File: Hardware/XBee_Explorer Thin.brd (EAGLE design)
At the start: 43.2 x 52.1 mm, 65 parts, among them J4 QWIIC_RIGHT_ANGLE, Q2 3.1A/30V/105mΩ, U1 FSUSB30MUX_MSOP10, U2 AP63203, U3 ESD Diode, U5 ESD Diode, U6 CP210X

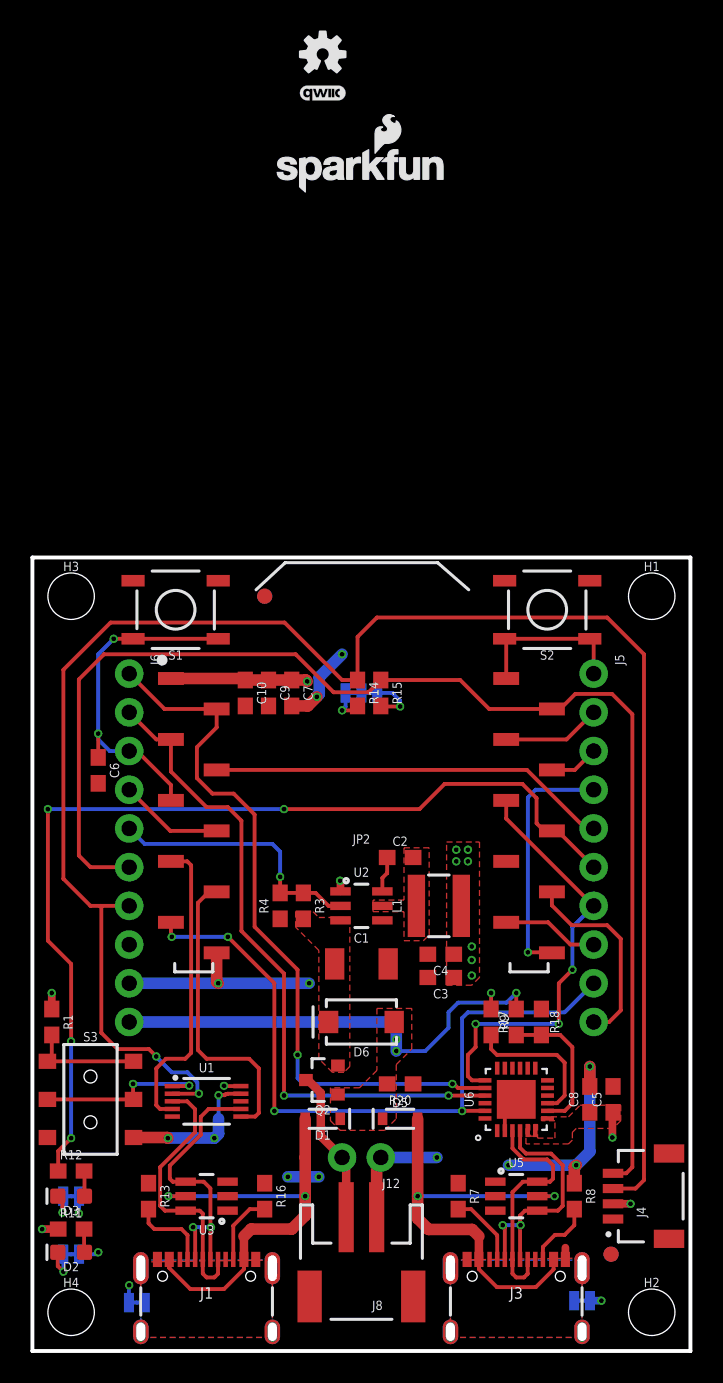
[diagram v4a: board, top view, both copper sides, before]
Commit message: Improves the ground pour significantly
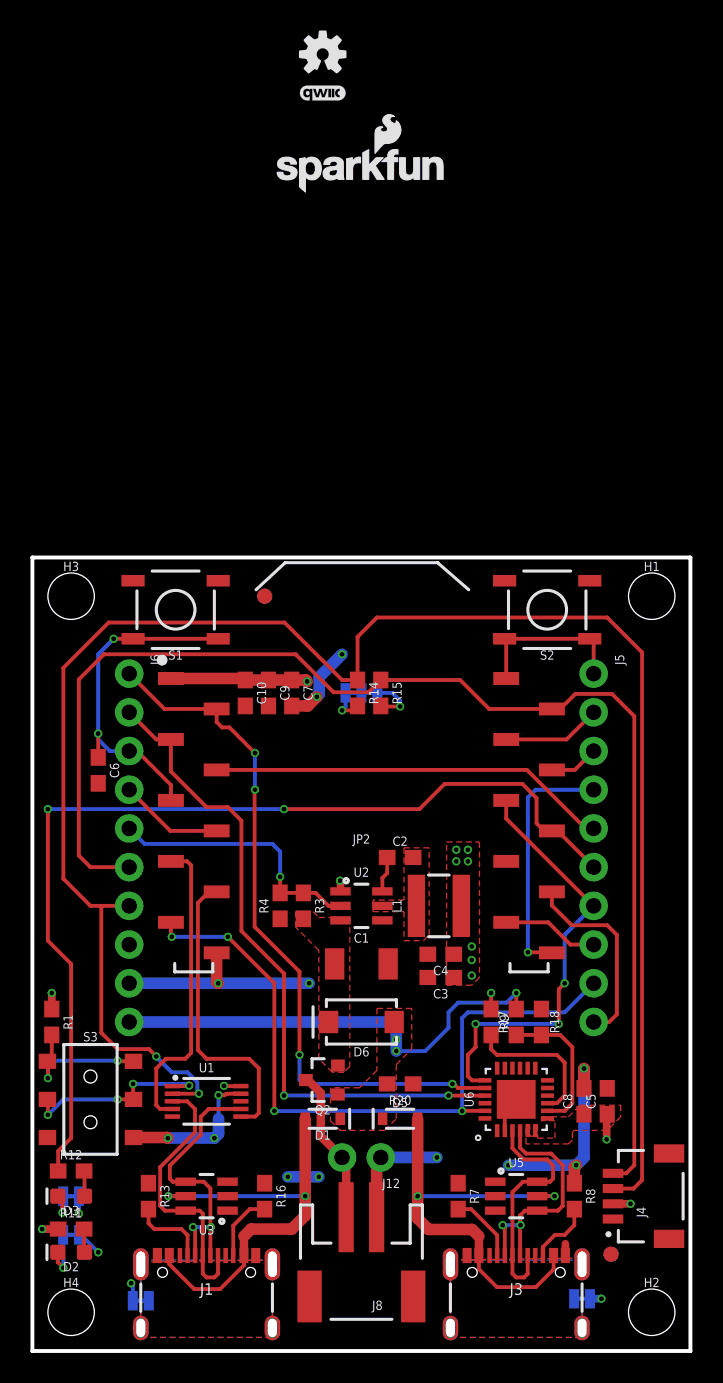
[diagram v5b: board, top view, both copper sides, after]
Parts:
- moved JP1 1.27 mm to (2.54, 7.62)
- moved C5 0.40 mm to (37.7, 16.4)
- moved C8 0.40 mm to (36.2, 16.4)
- moved SHLD1 0.28 mm to (7.11, 3.30)
- moved J1 0.25 mm to (11.4, 6.60)
- moved J3 0.25 mm to (31.8, 6.60)
- moved SHLD 0.13 mm to (36.1, 3.43)
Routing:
- net N$3: track 7.50 -> 9.46 mm, vias 0 -> 2
- net DIRECT_SELECT: track 11.6 -> 13.3 mm, vias 2 -> 4
- net D13/TXO: track 47.6 -> 46.0 mm, vias 2 -> 4
- net N$23: track 2.57 -> 3.33 mm
- net DIRECT_D-: track 18.7 -> 18.2 mm
- net D-: track 16.5 -> 16.0 mm
- net D5/ASSOCIATE: vias 4 -> 2

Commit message: Few more improvements
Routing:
- net GND: track 60.3 -> 61.8 mm, vias 17 -> 18
- net VIN: track 30.3 -> 31.0 mm, vias 3 -> 4
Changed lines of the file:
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@@
 <wire x1="10.8204" y1="17.63734375" x2="10.16974375" y2="18.288" width="0.254" layer="16"/>
 <wire x1="10.16974375" y1="18.288" x2="9.144" y2="18.288" width="0.254" layer="16"/>
-<wire x1="9.144" y1="18.288" x2="8.128" y2="19.304" width="0.254" layer="16"/>
-<wire x1="8.128" y1="19.304" x2="8.128" y2="19.3294" width="0.254" layer="16"/>
-<via x="8.128" y="19.3294" extent="1-16" drill="0.3048"/>
+<wire x1="9.144" y1="18.288" x2="8.001" y2="19.431" width="0.254" layer="16"/>
+<wire x1="8.001" y1="19.431" x2="8.001" y2="19.4564" width="0.254" layer="16"/>
+<via x="8.001" y="19.4564" extent="1-16" drill="0.3048"/>
 <contactref element="J6" pad="7"/>
 <wire x1="6.35" y1="29.21" x2="4.445" y2="29.21" width="0.254" layer="1"/>
 <wire x1="4.445" y1="29.21" x2="3.81" y2="29.21" width="0.254" layer="1"/>
 <wire x1="3.81" y1="29.21" x2="2.032" y2="30.988" width="0.254" layer="1"/>
-<wire x1="8.128" y1="19.3294" x2="7.6454" y2="19.812" width="0.254" layer="1"/>
+<wire x1="8.001" y1="19.4564" x2="7.6454" y2="19.812" width="0.254" layer="1"/>
 <wire x1="7.6454" y1="19.812" x2="5.588" y2="19.812" width="0.254" layer="1"/>
 <wire x1="5.588" y1="19.812" x2="4.5212" y2="20.8788" width="0.254" layer="1"/>
@@
 <via x="18.161" y="24.13" extent="1-16" drill="0.3048"/>
 <wire x1="13.68" y1="16.883" x2="12.81134375" y2="16.883" width="0.254" layer="1"/>
-<wire x1="12.81134375" y1="16.883" x2="12.79394375" y2="16.8656" width="0.254" layer="1"/>
-<wire x1="12.79394375" y1="16.8656" x2="12.7" y2="16.8656" width="0.254" layer="1"/>
 <wire x1="6.635" y1="14.01" x2="8.85" y2="14.01" width="0.762" layer="1"/>
 <wire x1="8.85" y1="14.01" x2="8.89" y2="13.97" width="0.762" layer="1"/>
@@
 <wire x1="8.89" y1="13.97" x2="11.938" y2="13.97" width="0.762" layer="16"/>
 <via x="11.938" y="13.97" extent="1-16" drill="0.3048"/>
-<wire x1="12.7" y1="16.8656" x2="12.621465625" y2="16.787065625" width="0.254" layer="1"/>
-<wire x1="12.621465625" y1="16.787065625" x2="12.215065625" y2="16.787065625" width="0.254" layer="1"/>
-<via x="12.215065625" y="16.787065625" extent="1-16" drill="0.3048"/>
-<wire x1="12.215065625" y1="16.787065625" x2="12.215065625" y2="15.24" width="0.254" layer="16"/>
 <via x="16.764" y="11.43" extent="1-16" drill="0.3048"/>
-<wire x1="12.215065625" y1="15.24" x2="12.215065625" y2="15.136065625" width="0.254" layer="16"/>
+<wire x1="12.215065625" y1="16.637" x2="12.215065625" y2="16.533065625" width="0.254" layer="16"/>
 <wire x1="16.764" y1="11.43" x2="18.796" y2="11.43" width="0.762" layer="16"/>
 <via x="18.796" y="11.43" extent="1-16" drill="0.3048"/>
@@
 <contactref element="J6" pad="9"/>
 <wire x1="12.192" y1="24.13" x2="6.35" y2="24.13" width="0.762" layer="16"/>
-<wire x1="17.018" y1="42.33" x2="18.073" y2="42.33" width="0.762" layer="1"/>
-<wire x1="18.073" y1="42.33" x2="18.669" y2="42.926" width="0.762" layer="1"/>
-<via x="18.669" y="42.926" extent="1-16" drill="0.3048"/>
-<via x="20.32" y="45.72" extent="1-16" drill="0.3048"/>
-<wire x1="18.669" y1="42.926" x2="18.669" y2="42.95544375" width="0.762" layer="16"/>
-<wire x1="18.669" y1="42.95544375" x2="18.8214" y2="43.10784375" width="0.762" layer="16"/>
-<wire x1="18.8214" y1="43.10784375" x2="18.8214" y2="44.2214" width="0.762" layer="16"/>
-<wire x1="18.8214" y1="44.2214" x2="20.32" y2="45.72" width="0.762" layer="16"/>
-<wire x1="12.215065625" y1="15.24" x2="12.215065625" y2="14.247065625" width="0.762" layer="16"/>
+<wire x1="12.215065625" y1="14.247065625" x2="12.215065625" y2="16.637" width="0.762" layer="16"/>
 <wire x1="12.215065625" y1="14.247065625" x2="11.938" y2="13.97" width="0.762" layer="16"/>
+<via x="12.215065625" y="16.637" extent="1-16" drill="0.3048"/>
+<wire x1="12.81134375" y1="16.883" x2="12.79394375" y2="16.8656" width="0.254" layer="1"/>
+<wire x1="12.79394375" y1="16.8656" x2="12.443665625" y2="16.8656" width="0.254" layer="1"/>
+<wire x1="12.443665625" y1="16.8656" x2="12.215065625" y2="16.637" width="0.254" layer="1"/>
+<wire x1="25.947" y1="26.035" x2="26.416" y2="26.504" width="0.762" layer="1"/>
+<wire x1="26.416" y1="26.504" x2="26.416" y2="26.67" width="0.762" layer="1"/>
+<wire x1="26.67" y1="48.768" x2="26.67" y2="45.72" width="0.762" layer="16"/>
+<wire x1="26.67" y1="45.72" x2="26.67" y2="42.672" width="0.762" layer="16"/>
+<via x="26.67" y="45.72" extent="1-16" drill="0.3048"/>
+<via x="26.67" y="48.768" extent="1-16" drill="0.3048"/>
+<via x="26.67" y="42.672" extent="1-16" drill="0.3048"/>
 </signal>
 <signal name="3.3V">
@@
 <contactref element="JP2" pad="6"/>
 <contactref element="J6" pad="4"/>
-<wire x1="12.09" y1="34.13" x2="9.05" y2="34.13" width="0.254" layer="1"/>
-<wire x1="9.05" y1="34.13" x2="6.35" y2="36.83" width="0.254" layer="1"/>
+<wire x1="12.09" y1="34.13" x2="8.796" y2="34.13" width="0.254" layer="1"/>
+<wire x1="8.796" y1="34.13" x2="6.35" y2="36.576" width="0.254" layer="1"/>
+<wire x1="6.35" y1="36.576" x2="6.35" y2="36.83" width="0.254" layer="1"/>
 </signal>
 <signal name="D8/!DTR!">
@@
 <wire x1="34.09" y1="30.13" x2="34.09" y2="29.241" width="0.254" layer="1"/>
 <wire x1="35.391" y1="27.94" x2="37.719" y2="27.94" width="0.254" layer="1"/>
-<wire x1="37.719" y1="27.94" x2="38.354" y2="27.305" width="0.254" layer="1"/>
-<wire x1="38.354" y1="27.305" x2="38.354" y2="22.098" width="0.254" layer="1"/>
-<wire x1="38.354" y1="22.098" x2="37.846" y2="21.59" width="0.254" layer="1"/>
+<wire x1="37.719" y1="27.94" x2="38.481" y2="27.178" width="0.254" layer="1"/>
+<wire x1="38.481" y1="27.178" x2="38.481" y2="22.225" width="0.254" layer="1"/>
+<wire x1="38.481" y1="22.225" x2="37.846" y2="21.59" width="0.254" layer="1"/>
 <wire x1="37.846" y1="21.59" x2="36.83" y2="21.59" width="0.254" layer="1"/>
 </signal>
@@
 <wire x1="34.09" y1="34.13" x2="33.582" y2="34.13" width="0.254" layer="1"/>
 <wire x1="33.582" y1="34.13" x2="33.083" y2="34.629" width="0.254" layer="1"/>
-<wire x1="33.083" y1="34.629" x2="33.083" y2="36.2792125" width="0.254" layer="1"/>
-<wire x1="32.1512125" y1="37.211" x2="33.083" y2="36.2792125" width="0.254" layer="1"/>
+<wire x1="33.083" y1="34.629" x2="33.083" y2="36.4062125" width="0.254" layer="1"/>
+<wire x1="32.2782125" y1="37.211" x2="33.083" y2="36.4062125" width="0.254" layer="1"/>
 <via x="16.51" y="35.56" extent="1-16" drill="0.3048"/>
 <wire x1="16.51" y1="35.56" x2="1.016" y2="35.56" width="0.254" layer="16"/>
 <via x="1.016" y="35.56" extent="1-16" drill="0.3048"/>
-<wire x1="1.016" y1="35.56" x2="1.016" y2="26.924" width="0.254" layer="1"/>
-<wire x1="1.016" y1="26.924" x2="2.54" y2="25.4" width="0.254" layer="1"/>
+<wire x1="1.016" y1="35.56" x2="1.016" y2="29.972" width="0.254" layer="1"/>
+<wire x1="1.016" y1="29.972" x2="2.54" y2="28.448" width="0.254" layer="1"/>
 <wire x1="2.54" y1="13.97" x2="1.69" y2="13.12" width="0.254" layer="1"/>
 <wire x1="1.69" y1="13.12" x2="1.69" y2="11.811" width="0.254" layer="1"/>
 <wire x1="16.51" y1="35.56" x2="25.4" y2="35.56" width="0.254" layer="1"/>
 <wire x1="25.4" y1="35.56" x2="27.051" y2="37.211" width="0.254" layer="1"/>
-<wire x1="27.051" y1="37.211" x2="32.1512125" y2="37.211" width="0.254" layer="1"/>
-<wire x1="2.54" y1="25.4" x2="2.54" y2="13.97" width="0.254" layer="1"/>
+<wire x1="27.051" y1="37.211" x2="32.2782125" y2="37.211" width="0.254" layer="1"/>
+<wire x1="2.54" y1="28.448" x2="2.54" y2="13.97" width="0.254" layer="1"/>
 </signal>
 <signal name="D6/!RTS!">
@@
 <wire x1="9.18" y1="15.883" x2="8.374" y2="15.883" width="0.254" layer="1"/>
 <wire x1="8.374" y1="15.883" x2="8.128" y2="16.129" width="0.254" layer="1"/>
-<wire x1="8.128" y1="16.129" x2="8.128" y2="18.542" width="0.254" layer="1"/>
+<wire x1="8.128" y1="16.129" x2="8.128" y2="18.034" width="0.254" layer="1"/>
 <wire x1="9.78" y1="32.13" x2="9.779" y2="32.131" width="0.254" layer="1"/>
-<wire x1="8.763" y1="19.177" x2="10.033" y2="19.177" width="0.254" layer="1"/>
+<wire x1="9.271" y1="19.177" x2="10.033" y2="19.177" width="0.254" layer="1"/>
 <wire x1="10.033" y1="19.177" x2="10.414" y2="19.558" width="0.254" layer="1"/>
-<wire x1="8.128" y1="18.542" x2="8.763" y2="19.177" width="0.254" layer="1"/>
+<wire x1="8.128" y1="18.034" x2="9.271" y2="19.177" width="0.254" layer="1"/>
 <wire x1="10.414" y1="19.558" x2="10.414" y2="31.877" width="0.254" layer="1"/>
 <wire x1="9.09" y1="32.13" x2="9.78" y2="32.13" width="0.254" layer="1"/>
@@
 <wire x1="13.68" y1="15.383" x2="14.621" y2="15.383" width="0.254" layer="1"/>
 <wire x1="14.621" y1="15.383" x2="14.859" y2="15.621" width="0.254" layer="1"/>
-<wire x1="14.859" y1="15.621" x2="14.859" y2="18.542" width="0.254" layer="1"/>
-<wire x1="14.224" y1="19.177" x2="11.43" y2="19.177" width="0.254" layer="1"/>
+<wire x1="14.859" y1="15.621" x2="14.859" y2="18.034" width="0.254" layer="1"/>
+<wire x1="13.716" y1="19.177" x2="11.43" y2="19.177" width="0.254" layer="1"/>
 <wire x1="11.582" y1="30.13" x2="12.09" y2="30.13" width="0.254" layer="1"/>
 <wire x1="11.582" y1="30.13" x2="10.859" y2="29.407" width="0.254" layer="1"/>
-<wire x1="14.859" y1="18.542" x2="14.224" y2="19.177" width="0.254" layer="1"/>
+<wire x1="14.859" y1="18.034" x2="13.716" y2="19.177" width="0.254" layer="1"/>
 <wire x1="10.859" y1="29.407" x2="10.859" y2="19.748" width="0.254" layer="1"/>
 <wire x1="10.859" y1="19.748" x2="11.43" y2="19.177" width="0.254" layer="1"/>
@@
 <contactref element="R17" pad="2"/>
 <polygon width="0.127" layer="1" isolate="0.3048" thermals="no">
-<vertex x="20.193" y="14.478"/>
-<vertex x="23.114" y="14.478"/>
+<vertex x="19.939" y="14.732"/>
+<vertex x="23.368" y="14.732"/>
 <vertex x="23.876" y="15.24"/>
 <vertex x="23.876" y="18.796"/>
@@
 <wire x1="25.781" y1="19.685" x2="27.305" y2="21.209" width="0.254" layer="16"/>
 <via x="23.876" y="20.447" extent="1-16" drill="0.3048"/>
+<wire x1="23.876" y1="19.685" x2="23.368" y2="19.177" width="0.762" layer="16"/>
+<via x="23.368" y="19.177" extent="1-16" drill="0.3048"/>
 </signal>
 <signal name="N$21">
